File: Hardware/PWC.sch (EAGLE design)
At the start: 45 parts, among them IC1 DS3502, IC2 DS3502, IC3 ESPWROOM32, IC5 CP2102N-A01-GQFN24, J1 OUTPUT, J2 USB-C-16P-16P, J3 BUT5, Q1 MMDT3904

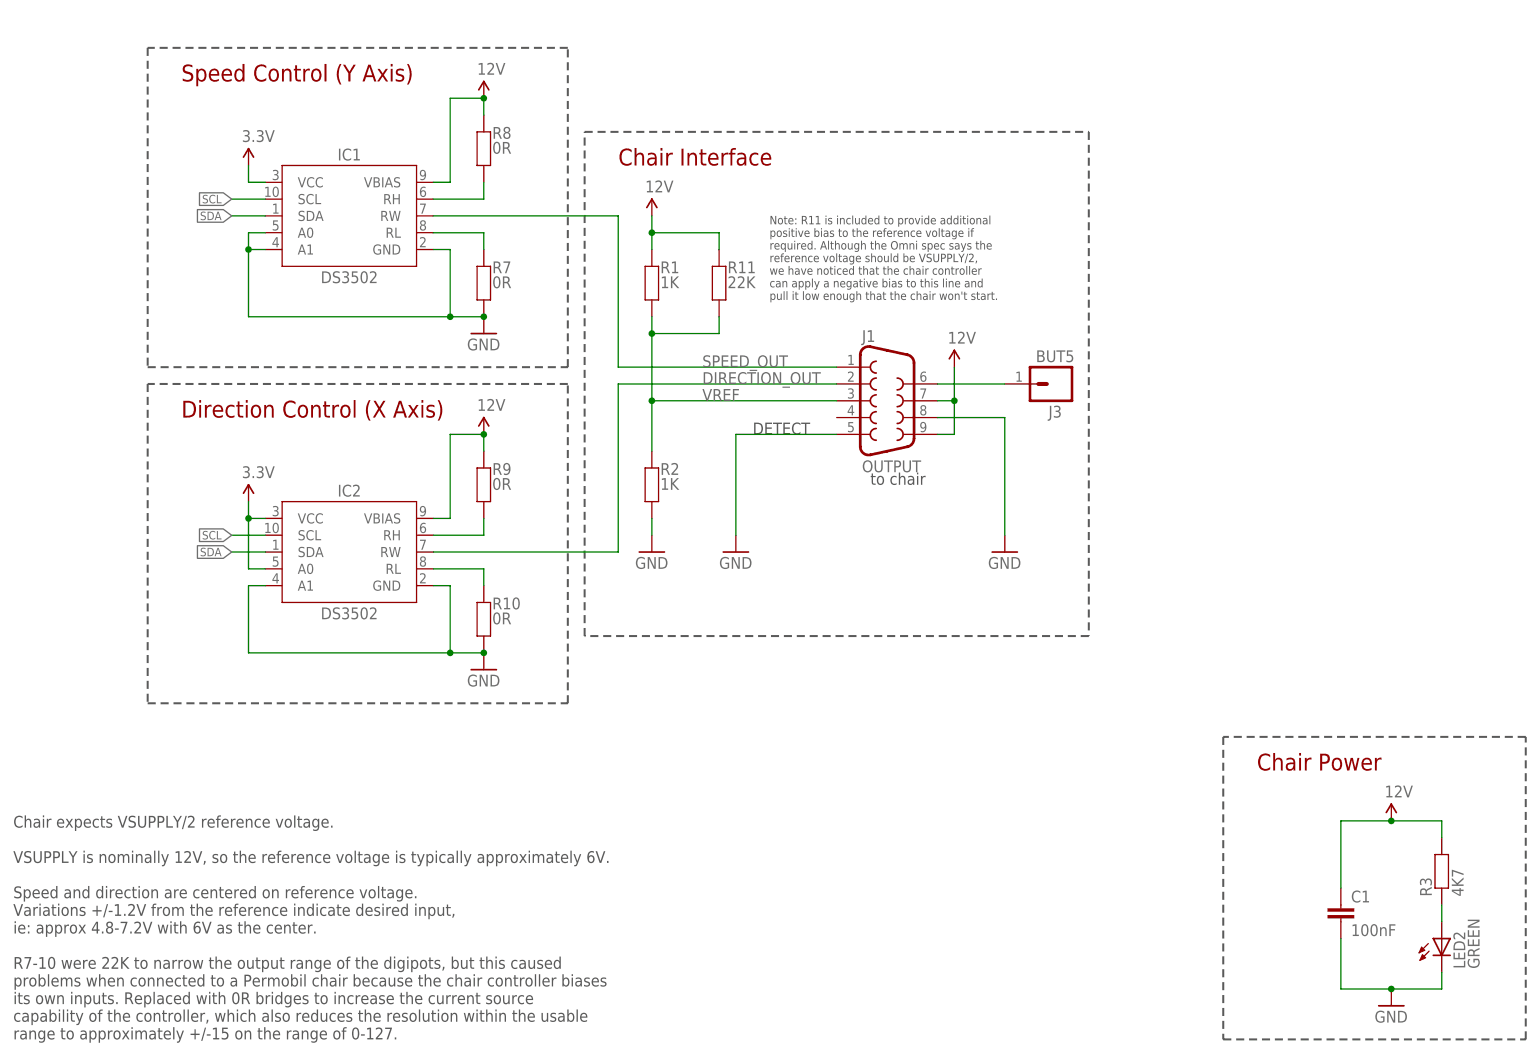
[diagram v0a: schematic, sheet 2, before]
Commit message: Routing, silkscreen, designators, ERC / DRC for v1.0 release.
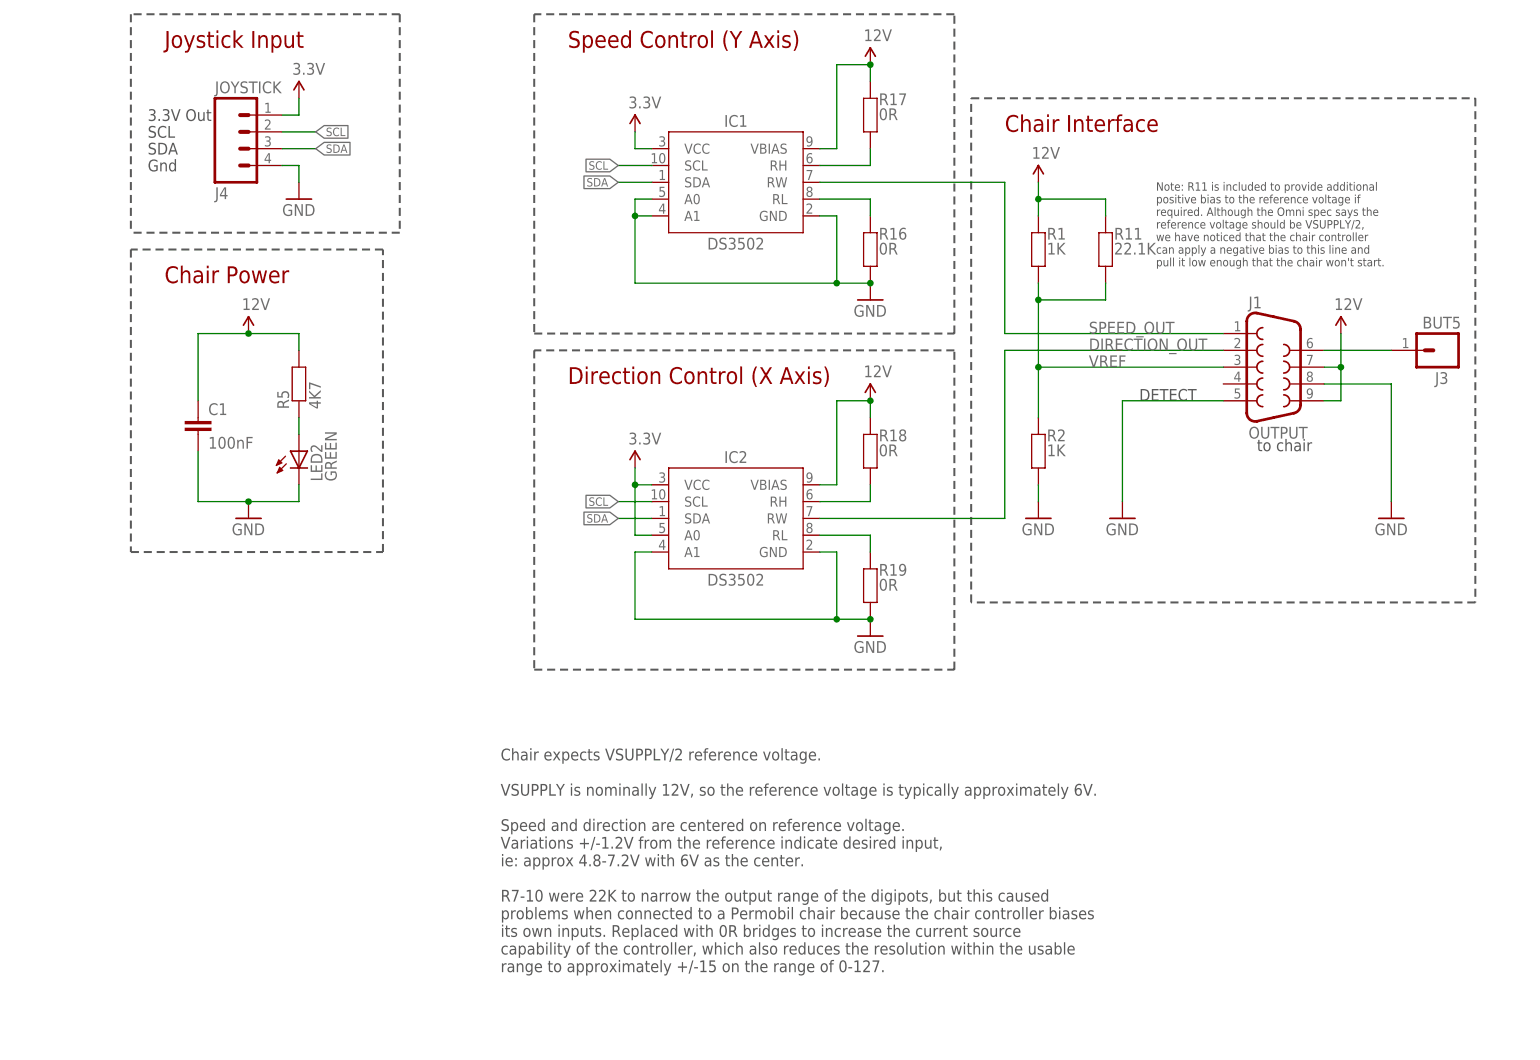
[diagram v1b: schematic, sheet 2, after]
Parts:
- removed LED5: TX/YEL, SuperHouse-LEDs:LED0603
- removed R20: 47.5K, SuperHouse-DiscreteSemi:RESISTOR0603
- removed R21: 1K, SuperHouse-DiscreteSemi:RESISTOR0603
- added J4: JOYSTICK, SuperHouse-Connectors:M04-PLAIN
- added LED1: BLUE, SuperHouse-LEDs:LED0603
- added R12, R13: 22.1K, SuperHouse-DiscreteSemi:RESISTOR0603
- LED3: value BLUE -> TX/YEL
- R10, R8, R9: value 0R -> 10K
- R11: value 22K -> 22.1K
- R14: value 10K -> 22.1K
- R15: value 10K -> 47.5K
- R16: value 5.1K -> 0R
- R17, R18: value 22K -> 0R
- R19: value 22.1K -> 0R
- R3: value 4K7 -> 1K
- R5: value 10K -> 4K7
- R7: value 0R -> 5.1K
- renumbered C7 to C3, C8 to C2, IC5 to IC4, R22 to R4, S2 to S1
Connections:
- net !RESET: now also R12.2; no longer R17.2
- net 12V: now also R17.2, R18.2, R5.2; no longer R3.2, R8.2, R9.2
- net 3.3V: now also J4.1, LED3.A, R10.2, R12.1, R13.1; no longer LED5.A, R17.1, R18.1, R5.2
- net 5V: now also R14.2; no longer R19.2
- net DTR: now also R8.1; no longer R14.1
- net GND: now also J4.4, LED1.C, R15.1, R19.1; no longer LED3.C, R10.1, R20.1
- net GPIO0: now also R13.2; no longer R18.2
- net N$1: now also LED1.A, R10.1; no longer LED3.A, R5.1
- net N$10: now also R7.2; no longer R16.2
- net N$13: now also LED3.C; no longer LED5.C
- net N$15: now also R19.2; no longer R10.2
- net N$2: now also R17.1; no longer R8.1
- net N$3: now also R18.1; no longer R9.1
- net N$39: now also R14.1, R15.2; no longer R19.1, R20.2
- net N$4: now also R16.2; no longer R7.2
- net N$6: now also R5.1; no longer R3.1
- net N$7: now also R8.2; no longer R14.2
- net N$8: now also R9.2; no longer R15.2
- net N$9: now also R3.2; no longer R21.2
- net RTS: now also R9.1; no longer R15.1
- net RX_LED: now also R3.1; no longer R21.1
- net SCL: now also J4.2
- net SDA: now also J4.3
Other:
- note added: "3.3V Out"
- note added: "GPIO0: GPIO1: USB_TX GPIO2: GPIO3: USB_RX GPIO4: GPIO13: GPIO16: GPIO17: GPIO18: GPIO21: SDA GPIO22: SCL GPIO23: GPIO25: GPIO27: Firmware: https://github.com/SuperHouse/PWC"
- note added: "Gnd"
- note added: "I2C Addresses Y axis (speed): 0x28 X axis (direction): 0x29"
- note added: "Joystick Input"
- note added: "SCL"
- note added: "SDA"
- note removed: "GPIO0: GPIO1: USB_TX GPIO2: GPIO3: USB_RX GPIO4: GPIO13: GPIO16: GPIO17: GPIO18: GPIO21: SDA GPIO22: SCL GPIO23: GPIO25: GPIO27: Firmware: https://github.com/XXXXXX"
- note removed: "I2C Addresses X axis: 0x28 Y axis: 0x29"
- moved on the sheet: C1, IC1, IC2, J1, J3, LED2, LED3, R1, R11, R14, R15, R2
